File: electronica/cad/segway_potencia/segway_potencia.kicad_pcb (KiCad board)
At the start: 2 copper layers, 150 x 110 mm, 60 parts, among them J1 Batería MKDS3 1=P− 2=P+, J11 Motor IZQ 1=M+ 2=M−, J12 Motor DER 1=M+ 2=M−, J13 Servo IZQ JR, J14 Servo DER JR, J15 UBEC entrada, J16 UBEC salida 6V PT1,5 1=GND 2=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, J18 Voltímetro ROB-004, J20 Cable lógica-potencia 2x8, J3 Lazo interruptor+paro, Q1 IRF4905

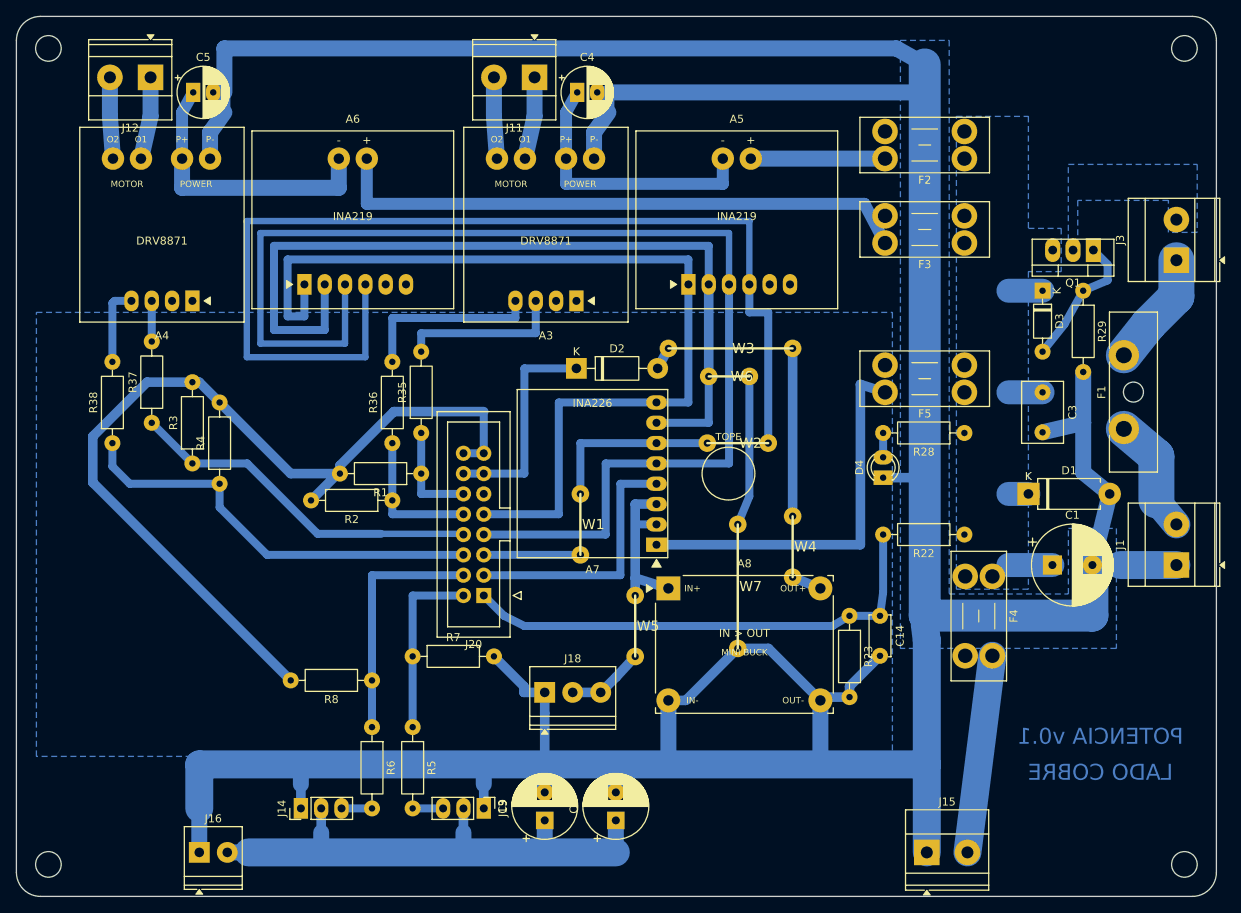
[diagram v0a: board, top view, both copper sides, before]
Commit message: electronica: rótulos de cobre, revisión independiente y control eléctrico (ELE-039)
- Rótulos de polaridad y de fusibles en el cobre de las dos placas,
  ubicados con ubicar_rotulos.py sin partir el relleno GND (SUP-14).
- Revisión independiente del conexionado contra las fichas: módulos,
  cable, polaridades y niveles correctos. Riesgos nuevos: A7 y A8 entran
  girados y queman (SUP-80), aleta de Q1 con tensión (SUP-20), I2C junto
  a PWM en el cable (SUP-81).
- auditoria_electrica.py: control repetible del sistema (cable, pines
  críticos, 5 V lejos de la ESP32, módulos girados, I2C, cuellos de
  pista, niveles). Informe: 0 fallas, 6 avisos.
- J26 reordenado con GND en el medio; textos de la Blue Pill en la
  especificación corregidos.
- ERC 0 y netlist coincidente; DRC 0/0/0 en las dos placas; salidas de
  fabricación regeneradas.

Co-Authored-By: Claude Opus 5.5 <noreply@anthropic.com>
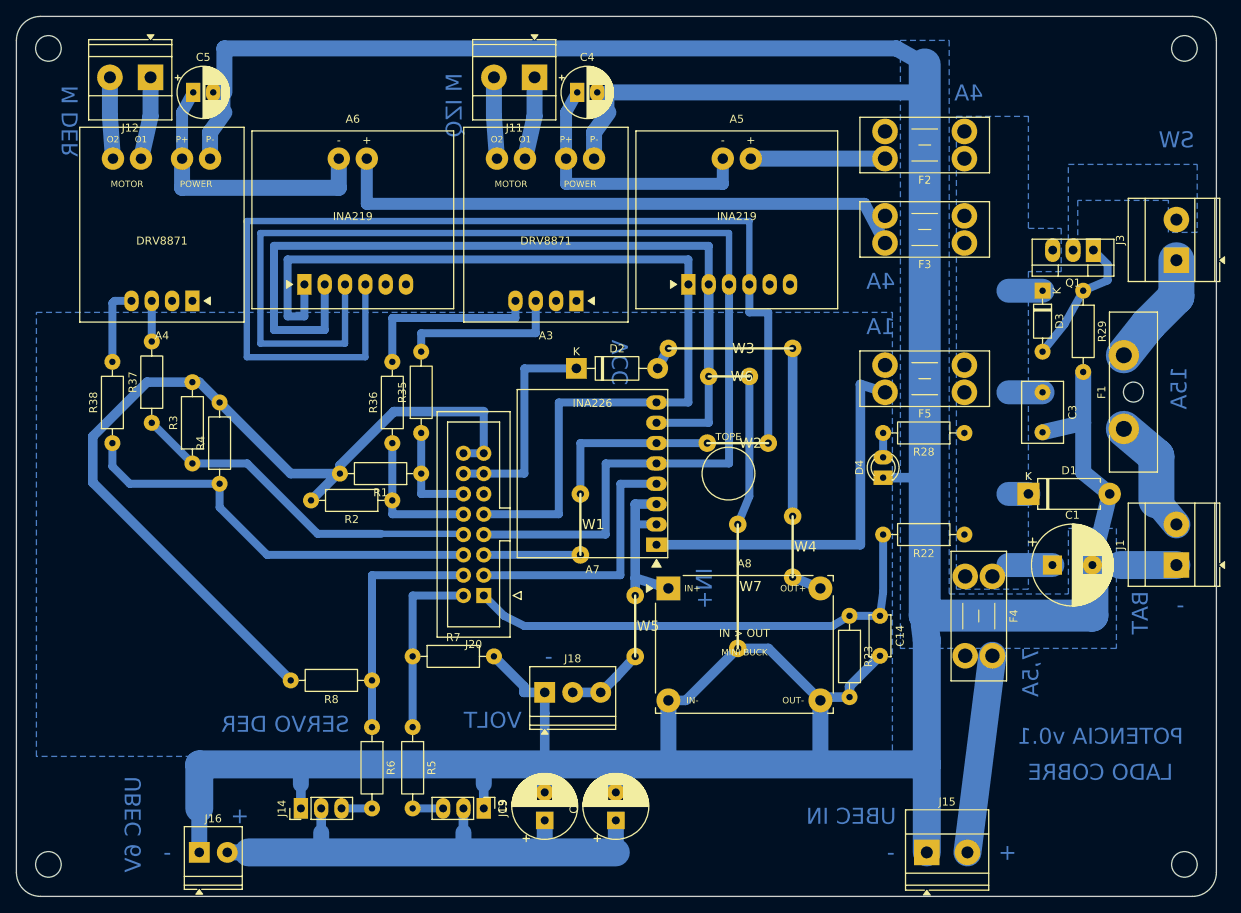
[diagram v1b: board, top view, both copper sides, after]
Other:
- board text added: "+"
- board text added: "-"
- board text added: "15A"
- board text added: "1A"
- board text added: "4A"
- board text added: "7,5A"
- board text added: "BAT"
- board text added: "IN+"
- board text added: "M DER"
- board text added: "M IZQ"
- board text added: "SERVO DER"
- board text added: "SW"
- board text added: "UBEC 6V"
- board text added: "UBEC IN"
- board text added: "VCC"
- board text added: "VOLT"

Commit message: electronica: PCB v0.2 de las dos placas, auditada (ELE-040)
- J3 y J4 pasan a pads para soldar el cable del interruptor y del paro.
- Montaje: A1-A4 en zócalo, A5-A8 soldados (DEC-20). A1 codificada:
  pin 24 cortado y posición tapada (revisión independiente: entraba
  girada o corrida y se quemaba).
- auditoria_electrica.py prueba giros y corrimientos de los módulos
  enchufados; 0 fallas, 3 avisos.
- Rótulos ambiguos de fusibles y VCC quitados; continuidad del cable
  J20 antes de enchufar; precinto en J3.
- Documentación v0.2, lista de compras, fabricación en rev-0.2.
- ERC 0, netlist coincidente, DRC 0/0/0 en las dos placas.

Co-Authored-By: Claude Opus 5.5 <noreply@anthropic.com>
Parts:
- J3: value Lazo interruptor+paro -> Interruptor+paro NC en serie, cable 1,5 mm² soldado; footprint TerminalBlock_Phoenix:TerminalBlock_Phoenix_MKDS-3-2-5.08_1x02_P5.08mm_Horizontal -> Connector_Wire:SolderWire-1.5sqmm_1x02_P6mm_D1.7mm_OD3mm
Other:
- board text added: "POTENCIA v0.2"
- board text removed: "1A"
- board text removed: "4A"
- board text removed: "POTENCIA v0.1"
- board text removed: "VCC"
